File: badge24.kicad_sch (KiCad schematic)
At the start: 23 parts, among them J1 SAO CONNECTOR, J2 SAO CONNECTOR, J3 SAO CONNECTOR, J4 SAO CONNECTOR, J5 SAO CONNECTOR, J6 SAO CONNECTOR, J7 Conn_01x09, J99 VEXT, M1 SC0918, SW11 SW_Push, SW22 SW_Push, SW33 SW_Push, T1 DMG2305

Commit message: clean up for writeup
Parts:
- BT1, BT2: footprint .stumbler:BatteryHolder_Keystone_2460_1xAA_SAO -> .badge24:BatteryHolder_Keystone_2460_1xAA_SAO; symbol Device:Battery_Cell -> .badge24:Battery_Cell
- J1, J2, J3, J4, J5, J6: footprint .stumbler:SAO_PIN_HEADER_2x03 -> .badge24:SAO_PIN_HEADER_2x03; symbol .stumbler:IO_JACK_F2x03B_SAO -> .badge24:IO_JACK_F2x03B_SAO
- J7: footprint .stumbler:IO_SAO_1x09_SMD_EXTERNAL -> .badge24:IO_SAO_1x09_SMD_EXTERNAL; symbol Connector_Generic:Conn_01x09 -> .badge24:Conn_01x09
- J99: footprint .stumbler:SAO_PinHeader_1x02_P2.54mm_SMD -> .badge24:SAO_PinHeader_1x02_P2.54mm_SMD; symbol .stumbler:IO_JACK_M02 -> .badge24:IO_JACK_M02
- JP1: footprint .stumbler:SolderJumper_Open_Rounded_SAO -> .badge24:SolderJumper_Open_Rounded_SAO; symbol Jumper:SolderJumper_3_Open -> .badge24:SolderJumper_3_Open
- LD1: footprint LED_SMD:LED_0805_2012Metric -> .badge24:LED_0805_2012Metric; symbol .stumbler:LED -> .badge24:LED
- M1: footprint .stumbler:RPi_Pico_SMD_SAO -> .badge24:RPi_Pico_SMD_SAO; symbol .stumbler:SC0918 -> .badge24:SC0918
- R1, R2, R3, R4, R5: footprint .stumbler:R_0603_1608Metric_SAO -> .badge24:R_0603_1608Metric_SAO; symbol .stumbler:RES -> .badge24:RES
- S1: footprint Button_Switch_THT:SW_Slide-03_Wuerth-WS-SLTV_10x2.5x6.4_P2.54mm -> .badge24:SW_Slide-03_Wuerth-WS-SLTV_10x2.5x6.4_P2.54mm; symbol .stumbler:SW_Slide_SPDT_SMALL -> .badge24:SW_Slide_SPDT_SMALL
- SW11, SW22, SW33: footprint .stumbler:SW_SPST_PTS645_SAO -> .badge24:SW_SPST_PTS645_SAO; symbol Switch:SW_Push -> .badge24:SW_Push
- T1: footprint .stumbler:SOT-23_SAO -> .badge24:SOT-23_SAO; symbol .stumbler:DMG2305 -> .badge24:DMG2305
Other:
- note added: "CHRIS LOTT THE STUMBLER"
- note added: "REDRAWN:"
- note added: "SAO1"
- note added: "SAO1~3"
- note added: "SAO2"
- note added: "SAO3"
- note added: "SAO4"
- note added: "SAO4~6"
- note added: "SAO5"
- note added: "SAO6"
- note removed: "REDRAWN: THE STUMBLER"
- company: (none) -> HACKADAY
- title: HACKADAY SUPERCON 2024, BADGE REDRAWN -> SUPERCON 2024
- moved on the sheet: BT1, BT2, J7, JP1, LD1, M1, R1, R2, R3, R4, R5, S1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

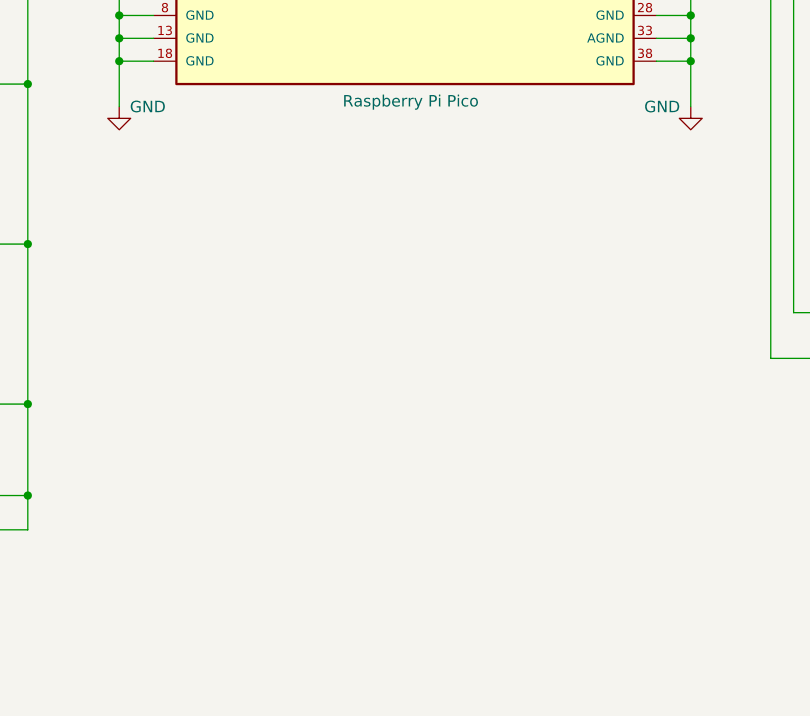
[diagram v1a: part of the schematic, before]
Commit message: added original schematic sheet
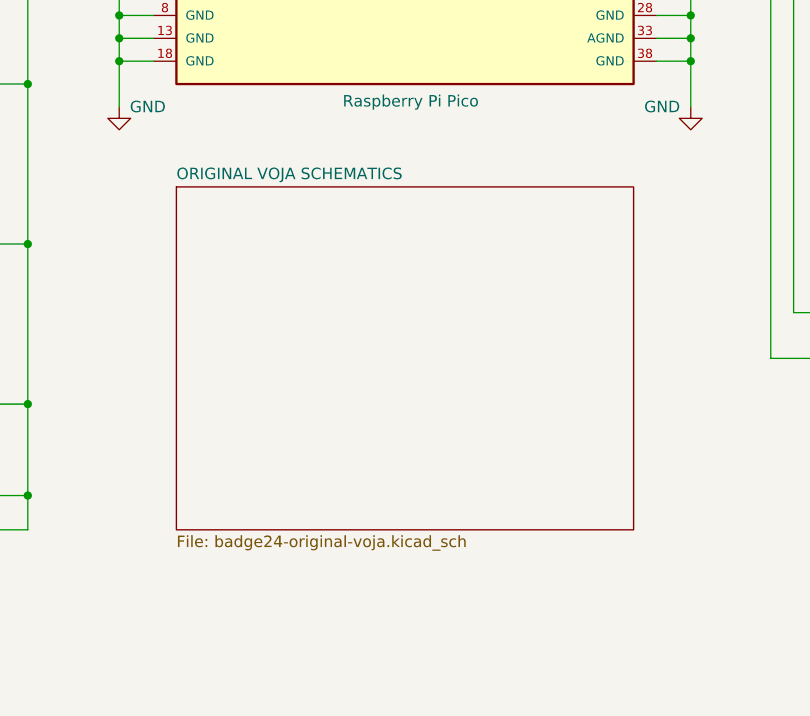
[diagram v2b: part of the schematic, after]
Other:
- added sheet ORIGINAL VOJA SCHEMATICS (badge24-original-voja.kicad_sch)
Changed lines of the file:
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@@
+		)
+	)
+	(sheet
+		(at 121.92 118.11)
+		(size 50.8 38.1)
+		(fields_autoplaced yes)
+		(stroke
+			(width 0.1524)
+			(type solid)
+		)
+		(fill
+			(color 0 0 0 0.0000)
+		)
+		(property "Sheetname" "ORIGINAL VOJA SCHEMATICS"
+			(at 121.92 117.3984 0)
+			(effects
+				(font
+					(size 1.27 1.27)
+				)
+				(justify left bottom)
+			)
+		)
+		(property "Sheetfile" "badge24-original-voja.kicad_sch"
+			(at 121.92 156.7946 0)
+			(effects
+				(font
+					(size 1.27 1.27)
+				)
+				(justify left top)
+			)
+		)
+		(instances
+			(project "badge24"
+				(path "/6f5575ee-d8e7-41b5-a202-c1cbb928830a"
+					(page "2")
+				)
+			)
 		)
 	)

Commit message: added jolly wrencher
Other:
- company: HACKADAY -> (none)
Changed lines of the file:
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@@
 		(date "2024-10-30")
 		(rev "A")
-		(company "HACKADAY")
 		(comment 1 "BADGE REDRAWN")
 		(comment 2 "SCHEMATIC")
@@
 	)
 	(symbol
+		(lib_id ".badge24:HACKADAY_TEXT")
+		(at 123.19 190.5 0)
+		(unit 1)
+		(exclude_from_sim yes)
+		(in_bom no)
+		(on_board no)
+		(dnp no)
+		(fields_autoplaced yes)
+		(property "Reference" "#G2"
+			(at 123.19 185.1451 0)
+			(effects
+				(font
+					(size 1.27 1.27)
+				)
+				(hide yes)
+			)
+		)
+		(property "Value" "HACKADAY_TEXT"
+			(at 123.19 195.8549 0)
+			(effects
+				(font
+					(size 1.27 1.27)
+				)
+				(hide yes)
+			)
+		)
+		(property "Footprint" ""
+			(at 123.19 190.5 0)
+			(effects
+				(font
+					(size 1.27 1.27)
+				)
+				(hide yes)
+			)
+		)
+		(property "Datasheet" ""
+			(at 123.19 190.5 0)
+			(effects
+				(font
+					(size 1.27 1.27)
+				)
+				(hide yes)
+			)
+		)
+		(property "Description" ""
+			(at 123.19 190.5 0)
+			(effects
+				(font
+					(size 1.27 1.27)
+				)
+				(hide yes)
+			)
+		)
+		(instances
+			(project ""
+				(path "/6f5575ee-d8e7-41b5-a202-c1cbb928830a"
+					(reference "#G2")
+					(unit 1)
+				)
+			)
+		)
+	)
+	(symbol
 		(lib_id ".badge24:Conn_01x09")
 		(at 50.8 49.53 0)
@@
 					(unit 1)
 				)
+			)
+		)
+	)
+	(symbol
+		(lib_id ".badge24:HACKADAY_LOGO")
+		(at 91.44 185.42 0)
+		(unit 1)
+		(exclude_from_sim yes)
+		(in_bom no)
+		(on_board no)
+		(dnp no)
+		(fields_autoplaced yes)
+		(property "Reference" "#G1"
+			(at 91.44 173.355 0)
+			(effects
+				(font
+					(size 1.27 1.27)
+				)
+				(hide yes)
+			)
+		)
+		(property "Value" "HACKADAY_LOGO"
+			(at 91.44 197.485 0)
+			(effects
+				(font
+					(size 1.27 1.27)
+				)
+				(hide yes)
+			)
+		)
+		(property "Footprint" ""
+			(at 91.44 185.42 0)
+			(effects
+				(font
+					(size 1.27 1.27)
+				)
+				(hide yes)
+			)
+		)
+		(property "Datasheet" ""
+			(at 91.44 185.42 0)
+			(effects
+				(font
+					(size 1.27 1.27)
+				)
+				(hide yes)
+			)
+		)
+		(property "Description" ""
+			(at 91.44 185.42 0)
+			(effects
+				(font
+					(size 1.27 1.27)
+				)
+				(hide yes)
+			)
+		)
+		(instances
+			(project ""
+				(path "/6f5575ee-d8e7-41b5-a202-c1cbb928830a"
+					(reference "#G1")
+					(unit 1)
+				)
